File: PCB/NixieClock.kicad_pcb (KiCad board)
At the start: 2 copper layers, 146.7 x 95.2 mm, 49 parts, among them J1 12V, J3 Conn_01x03_Male, J4 Conn_01x03_Male, Q1 MPSA42, Q2 MPSA42, Q3 MPSA42, Q4 MPSA42, U1 L7805, U10 74141, U11 74141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

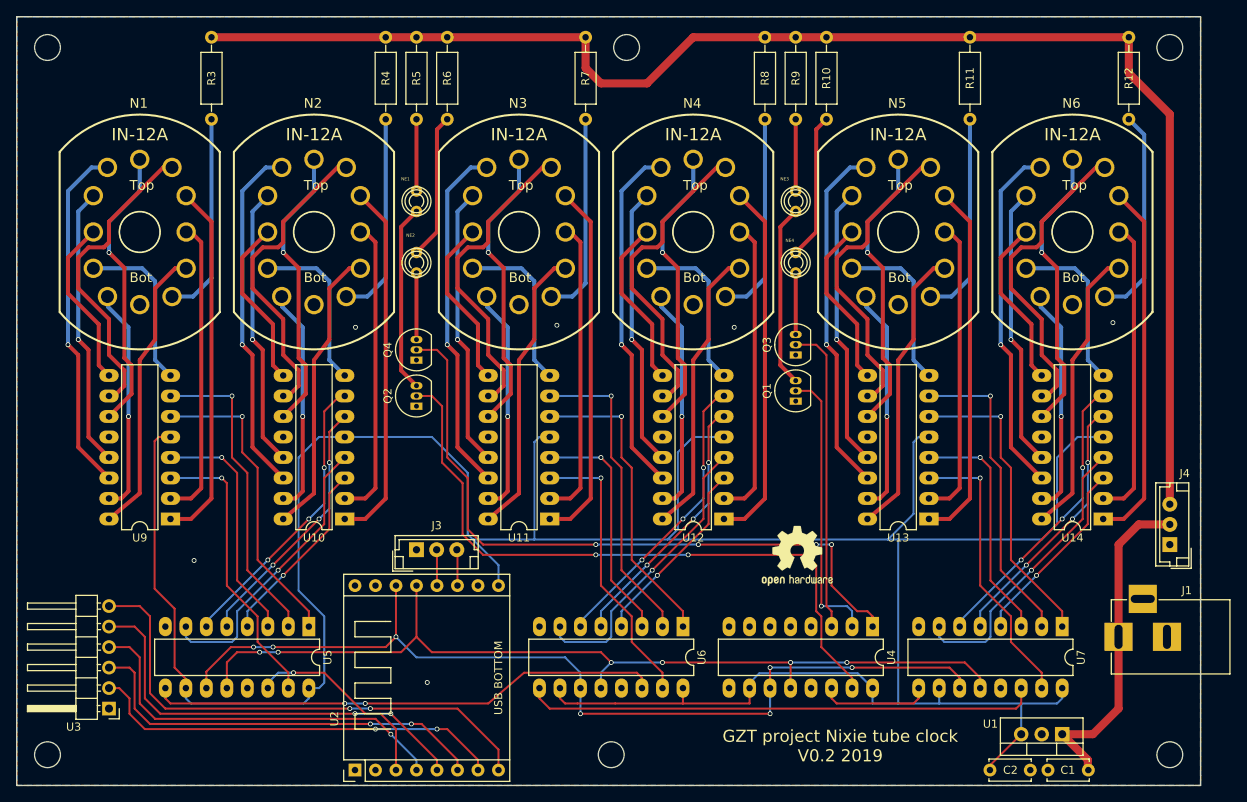
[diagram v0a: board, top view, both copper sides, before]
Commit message: Fixed issue #2 - added base resistors, layout touch-ups
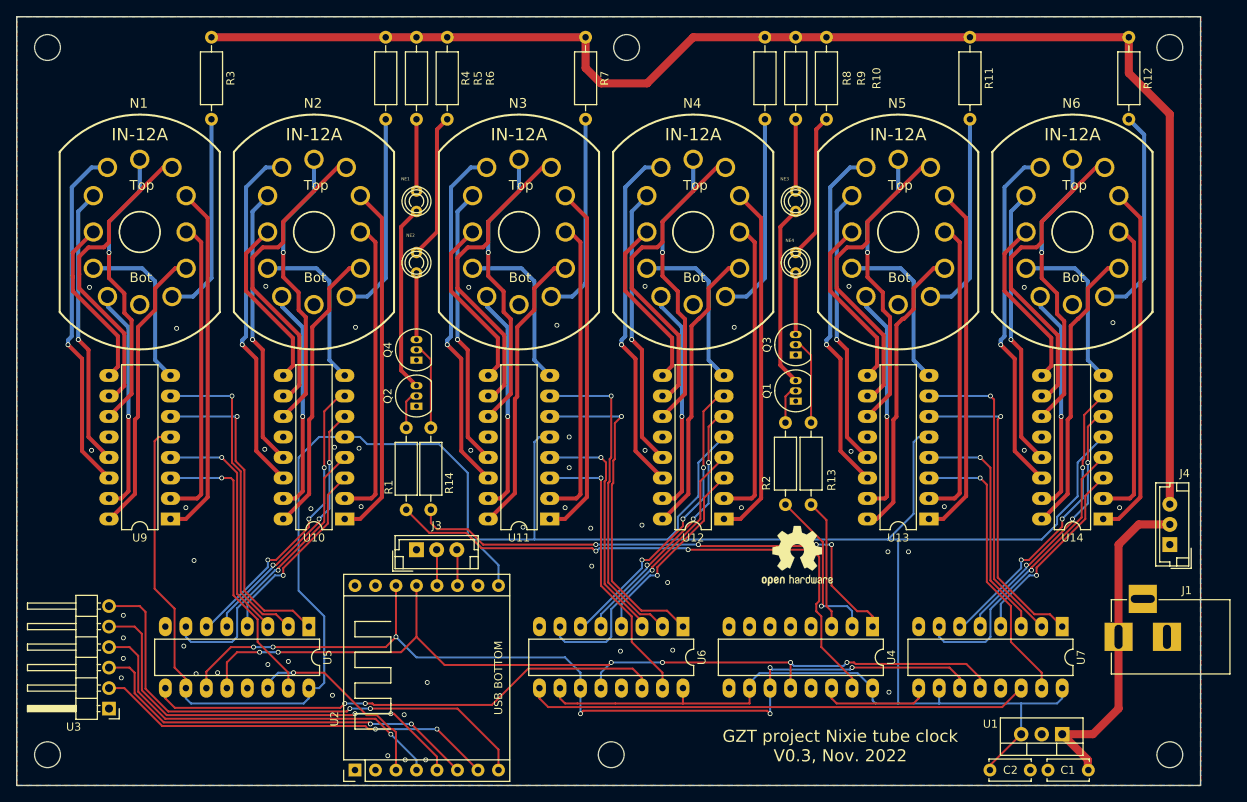
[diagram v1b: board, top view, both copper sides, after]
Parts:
- added R1: 2k2, Resistor_THT:R_Axial_DIN0207_L6.3mm_D2.5mm_P10.16mm_Horizontal, F.Cu at (121.9, 104.3)
- added R13: 2k2, Resistor_THT:R_Axial_DIN0207_L6.3mm_D2.5mm_P10.16mm_Horizontal, F.Cu at (172.1, 103.6)
- added R14: 2k2, Resistor_THT:R_Axial_DIN0207_L6.3mm_D2.5mm_P10.16mm_Horizontal, F.Cu at (125.0, 104.3)
- added R2: 2k2, Resistor_THT:R_Axial_DIN0207_L6.3mm_D2.5mm_P10.16mm_Horizontal, F.Cu at (168.9, 103.6)
- J1: value 12V -> Barrel_Jack
- R10, R11, R12, R3, R4, R5, R6, R7, R8, R9: footprint Resistors_THT:R_Axial_DIN0207_L6.3mm_D2.5mm_P10.16mm_Horizontal -> Resistor_THT:R_Axial_DIN0207_L6.3mm_D2.5mm_P10.16mm_Horizontal
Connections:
- net +5V renamed VCC
- U2 pad 1: Net-(U2-Pad1) -> unconnected-(U2-Pad1)
- U2 pad 15: Net-(U2-Pad15) -> unconnected-(U2-Pad15)
- U2 pad 16: Net-(U2-Pad16) -> unconnected-(U2-Pad16)
- U2 pad 2: Net-(U2-Pad2) -> unconnected-(U2-Pad2)
- U4 pad 1: Net-(Q4-Pad2) -> Net-(U4-Pad1)
- U4 pad 15: Net-(Q2-Pad2) -> Net-(U4-Pad15)
- U4 pad 2: Net-(Q1-Pad2) -> Net-(U4-Pad2)
- U4 pad 3: Net-(Q3-Pad2) -> Net-(U4-Pad3)
- U4 pad 4: Net-(U4-Pad4) -> unconnected-(U4-Pad4)
- U4 pad 5: Net-(U4-Pad5) -> unconnected-(U4-Pad5)
- U4 pad 6: Net-(U4-Pad6) -> unconnected-(U4-Pad6)
- U4 pad 7: Net-(U4-Pad7) -> unconnected-(U4-Pad7)
- U4 pad 9: Net-(U4-Pad9) -> unconnected-(U4-Pad9)
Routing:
- net Net-(Q2-Pad2): track 83.1 -> 4.80 mm, vias 2 -> 0
- net Net-(Q4-Pad2): track 85.2 -> 10.7 mm, vias 4 -> 0
- net Net-(U4-Pad15): track 0.00 -> 72.1 mm, vias 0 -> 2
- net Net-(U4-Pad1): track 0.00 -> 65.6 mm, vias 0 -> 4
- net Net-(Q1-Pad2): track 35.1 -> 4.80 mm, vias 1 -> 0
- net Net-(Q3-Pad2): track 38.3 -> 10.8 mm
- net Net-(U4-Pad2): track 0.00 -> 20.5 mm, vias 0 -> 1
- net Net-(U4-Pad3): track 0.00 -> 16.2 mm
- net VCC: track 365.4 -> 360.0 mm
- net Net-(U11-Pad6): track 38.1 -> 40.9 mm
- net Net-(U5-Pad1): track 38.3 -> 40.2 mm
- net Net-(U2-Pad7): track 51.8 -> 49.9 mm
- net Net-(U2-Pad6): track 51.8 -> 49.9 mm
- net Net-(U13-Pad6): track 38.1 -> 39.5 mm
- net Net-(U6-Pad9): track 63.7 -> 62.4 mm
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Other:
- net class 0.5 removed
- net class Default removed
- net class HV removed
- rule pad_to_mask_clearance: 0.2 -> 0
- board text added: "GZT project Nixie tube clock V0.3, Nov. 2022"
- board text removed: "GZT project Nixie tube clock V0.2 2019"
